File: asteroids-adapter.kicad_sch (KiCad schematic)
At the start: 15 parts, among them J1 Asteroids PCB connector, J2 Asteroids harness connector, U1 TL074

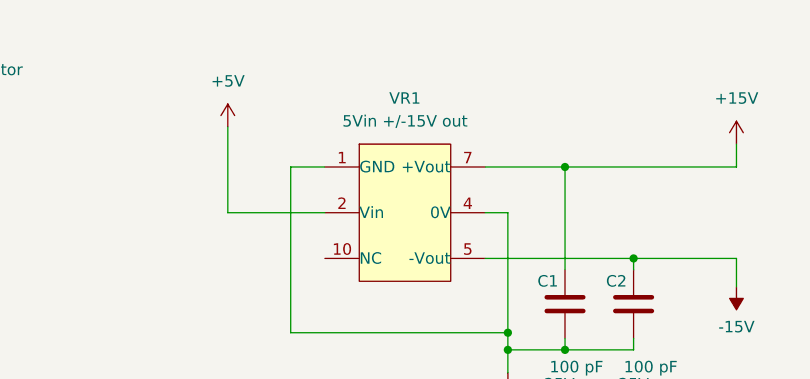
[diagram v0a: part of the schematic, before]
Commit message: Fixed DC-DC footprint and silk screen info
- Downloaded from CUI website

- fixed connector labels
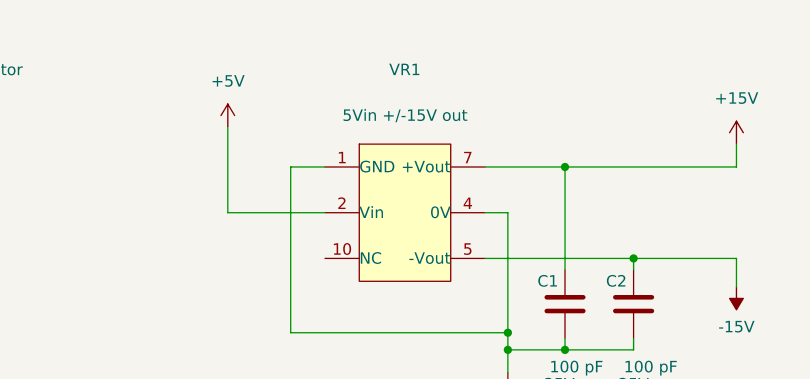
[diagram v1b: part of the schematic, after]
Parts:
- removed VR1: CUI PESE1-S5-D15-M 5V to +/-15V DC-DC converter 3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, asteroids-adapter:CUI PESE1 DC-DC dual out, symbol ast-adapter:CUI PESE1-S5-D15-M 5V to +/-15V DC-DC converter 34 mA
- added VR1: CUI PESE1-S5-D15-M, asteroids-adapter:CONV_PESE1-S5-D15-M, symbol ast-adapter:CUI PESE1-S5-D15-M
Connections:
- net +15V: now also VR1.7 (+Vout)
- net +5V: now also VR1.2 (Vin)
- net -15V: now also VR1.5 (-Vout)
- net GND: now also VR1.1 (GND), VR1.4 (0V)
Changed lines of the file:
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@@
     (pin "2")
-  )
-  (symbol (lib_id "ast-adapter:CUI PESE1-S5-D15-M 5V to +{slash}-15V DC-DC converter 34 mA") (at 151.765 34.925 0) (unit 1)
-    (in_bom yes) (on_board yes) (fields_autoplaced)
-    (property "Reference" "VR1" (id 0) (at 151.765 22.225 0))
-    (property "Value" "CUI PESE1-S5-D15-M 5V to +/-15V DC-DC converter 34 mA" (id 1) (at 126.365 140.843 0)
-      (effects (font (size 1.27 1.27)) (justify left) hide)
-    )
-    (property "Footprint" "asteroids-adapter:CUI PESE1 DC-DC dual out" (id 2) (at 151.765 22.225 0)
-      (effects (font (size 1.27 1.27)) hide)
-    )
-    (property "Datasheet" "https://www.google.com/url?sa=t&rct=j&q=&esrc=s&source=web&cd=&ved=2ahUKEwikiImr1v71AhUpk2oFHTgCD7YQFnoECAsQAQ&url=https%3A%2F%2Fwww.cui.com%2Fproduct%2Fresource%2Fpese1-m.pdf&usg=AOvVaw32_tGXML3NiDlAvSu1C1ul" (id 3) (at 128.143 135.509 0)
-      (effects (font (size 1.27 1.27)) hide)
-    )
-    (property "Component Value" "5Vin +/-15V out" (id 4) (at 151.765 24.765 0))
-    (property "Tolerance" "" (id 5) (at 132.207 145.669 0)
-      (effects (font (size 1.27 1.27)) hide)
-    )
-    (property "Manufacturer" "CUI" (id 6) (at 128.143 124.333 0)
-      (effects (font (size 1.27 1.27)) hide)
-    )
-    (property "Manufacturer Link" "https://www.cui.com/product/dc-dc-converters/isolated/pese1-m-series" (id 7) (at 130.937 130.937 0)
-      (effects (font (size 1.27 1.27)) hide)
-    )
-    (property "RoHS Document Link" "https://www.cui.com/product/resource/material-compliance/pese1-m-series" (id 8) (at 131.191 170.815 0)
-      (effects (font (size 1.27 1.27)) hide)
-    )
-    (property "Manufacturer PN" "PESE1-5S-D12-M" (id 9) (at 130.429 127.889 0)
-      (effects (font (size 1.27 1.27)) hide)
-    )
-    (property "RoHS" "Yes" (id 10) (at 127.889 168.021 0)
-      (effects (font (size 1.27 1.27)) hide)
-    )
-    (property "Allow Substitution" "No" (id 11) (at 127.635 173.863 0)
-      (effects (font (size 1.27 1.27)) hide)
-    )
-    (property "Fitted" "Yes" (id 12) (at 128.651 178.689 0)
-      (effects (font (size 1.27 1.27)) hide)
-    )
-    (property "Tracking" "No" (id 13) (at 128.143 176.149 0)
-      (effects (font (size 1.27 1.27)) hide)
-    )
-    (property "BOM Comment" "" (id 14) (at 154.305 106.045 0)
-      (effects (font (size 1.27 1.27)) hide)
-    )
-    (property "Component Type" "DC-DC converter" (id 15) (at 149.733 142.875 0)
-      (effects (font (size 1.27 1.27)) hide)
-    )
-    (property "Package Type" "SMT" (id 16) (at 116.205 121.285 0)
-      (effects (font (size 1.27 1.27)) hide)
-    )
-    (property "Package Variant" "" (id 17) (at 154.305 106.045 0)
-      (effects (font (size 1.27 1.27)) hide)
-    )
-    (property "Number of Pins" "If applicable" (id 18) (at 132.207 148.209 0)
-      (effects (font (size 1.27 1.27)) hide)
-    )
-    (property "Temp (Storage)" "If applicable" (id 19) (at 132.207 150.241 0)
-      (effects (font (size 1.27 1.27)) hide)
-    )
-    (property "Temp (Operating)" "If applicable" (id 20) (at 132.461 152.781 0)
-      (effects (font (size 1.27 1.27)) hide)
-    )
-    (property "Temp (Soldering)" "If applicable" (id 21) (at 132.461 155.575 0)
-      (effects (font (size 1.27 1.27)) hide)
-    )
-    (property "Temp Coeff." "If applicable" (id 22) (at 132.461 158.115 0)
-      (effects (font (size 1.27 1.27)) hide)
-    )
-    (property "Power Rating" "If applicable" (id 23) (at 132.461 160.655 0)
-      (effects (font (size 1.27 1.27)) hide)
-    )
-    (property "Material" "If applicable" (id 24) (at 132.461 162.941 0)
-      (effects (font (size 1.27 1.27)) hide)
-    )
-    (property "Class" "If applicable" (id 25) (at 132.461 165.227 0)
-      (effects (font (size 1.27 1.27)) hide)
-    )
-    (property "Standards Version" "1.1" (id 26) (at 128.651 181.737 0)
-      (effects (font (size 1.27 1.27)) hide)
-    )
-    (pin "1")
-    (pin "10")
-    (pin "2")
-    (pin "4")
-    (pin "5")
-    (pin "7")
   )
   (symbol (lib_id "power:GND") (at 104.775 170.18 0) (unit 1)
@@
     (pin "Z")
   )
+  (symbol (lib_id "ast-adapter:CUI PESE1-S5-D15-M") (at 151.765 34.925 0) (unit 1)
+    (in_bom yes) (on_board yes) (fields_autoplaced)
+    (property "Reference" "VR1" (id 0) (at 151.765 19.05 0))
+    (property "Value" "CUI PESE1-S5-D15-M" (id 1) (at 126.365 140.843 0)
+      (effects (font (size 1.27 1.27)) (justify left) hide)
+    )
+    (property "Footprint" "asteroids-adapter:CONV_PESE1-S5-D15-M" (id 2) (at 151.765 21.59 0)
+      (effects (font (size 1.27 1.27)) hide)
+    )
+    (property "Datasheet" "https://www.google.com/url?sa=t&rct=j&q=&esrc=s&source=web&cd=&ved=2ahUKEwikiImr1v71AhUpk2oFHTgCD7YQFnoECAsQAQ&url=https%3A%2F%2Fwww.cui.com%2Fproduct%2Fresource%2Fpese1-m.pdf&usg=AOvVaw32_tGXML3NiDlAvSu1C1ul" (id 3) (at 128.143 135.509 0)
+      (effects (font (size 1.27 1.27)) hide)
+    )
+    (property "Component Value" "5Vin +/-15V out" (id 4) (at 151.765 24.13 0))
+    (property "Tolerance" "" (id 5) (at 132.207 145.669 0)
+      (effects (font (size 1.27 1.27)) hide)
+    )
+    (property "Manufacturer" "CUI" (id 6) (at 128.143 124.333 0)
+      (effects (font (size 1.27 1.27)) hide)
+    )
+    (property "Manufacturer Link" "https://www.cui.com/product/dc-dc-converters/isolated/pese1-m-series" (id 7) (at 130.937 130.937 0)
+      (effects (font (size 1.27 1.27)) hide)
+    )
+    (property "RoHS Document Link" "https://www.cui.com/product/resource/material-compliance/pese1-m-series" (id 8) (at 131.191 170.815 0)
+      (effects (font (size 1.27 1.27)) hide)
+    )
+    (property "Manufacturer PN" "PESE1-5S-D12-M" (id 9) (at 130.429 127.889 0)
+      (effects (font (size 1.27 1.27)) hide)
+    )
+    (property "RoHS" "Yes" (id 10) (at 127.889 168.021 0)
+      (effects (font (size 1.27 1.27)) hide)
+    )
+    (property "Allow Substitution" "No" (id 11) (at 127.635 173.863 0)
+      (effects (font (size 1.27 1.27)) hide)
+    )
+    (property "Fitted" "Yes" (id 12) (at 128.651 178.689 0)
+      (effects (font (size 1.27 1.27)) hide)
+    )
+    (property "Tracking" "No" (id 13) (at 128.143 176.149 0)
+      (effects (font (size 1.27 1.27)) hide)
+    )
+    (property "BOM Comment" "" (id 14) (at 154.305 106.045 0)
+      (effects (font (size 1.27 1.27)) hide)
+    )
+    (property "Component Type" "DC-DC converter" (id 15) (at 149.733 142.875 0)
+      (effects (font (size 1.27 1.27)) hide)
+    )
+    (property "Package Type" "SMT" (id 16) (at 116.205 121.285 0)
+      (effects (font (size 1.27 1.27)) hide)
+    )
+    (property "Package Variant" "" (id 17) (at 154.305 106.045 0)
+      (effects (font (size 1.27 1.27)) hide)
+    )
+    (property "Number of Pins" "If applicable" (id 18) (at 132.207 148.209 0)
+      (effects (font (size 1.27 1.27)) hide)
+    )
+    (property "Temp (Storage)" "If applicable" (id 19) (at 132.207 150.241 0)
+      (effects (font (size 1.27 1.27)) hide)
+    )
+    (property "Temp (Operating)" "If applicable" (id 20) (at 132.461 152.781 0)
+      (effects (font (size 1.27 1.27)) hide)
+    )
+    (property "Temp (Soldering)" "If applicable" (id 21) (at 132.461 155.575 0)
+      (effects (font (size 1.27 1.27)) hide)
+    )
+    (property "Temp Coeff." "If applicable" (id 22) (at 132.461 158.115 0)
+      (effects (font (size 1.27 1.27)) hide)
+    )
+    (property "Power Rating" "If applicable" (id 23) (at 132.461 160.655 0)
+      (effects (font (size 1.27 1.27)) hide)
+    )
+    (property "Material" "If applicable" (id 24) (at 132.461 162.941 0)
+      (effects (font (size 1.27 1.27)) hide)
+    )
+    (property "Class" "If applicable" (id 25) (at 132.461 165.227 0)
+      (effects (font (size 1.27 1.27)) hide)
+    )
+    (property "Standards Version" "1.1" (id 26) (at 128.651 181.737 0)
+      (effects (font (size 1.27 1.27)) hide)
+    )
+    (pin "1")
+    (pin "10")
+    (pin "2")
+    (pin "4")
+    (pin "5")
+    (pin "7")
+  )
   (symbol (lib_id "ast-adapter:Yageo 10K ohm 1% thin film TH") (at 170.815 83.82 0) (unit 1)
     (in_bom yes) (on_board yes)
@@
       (reference "U1") (unit 5) (value "TL074") (footprint "Package_DIP:DIP-14_W7.62mm_LongPads")
     )
-    (path "/54237acd-3b11-4002-b44c-ec7678c2907b"
-      (reference "VR1") (unit 1) (value "CUI PESE1-S5-D15-M 5V to +/-15V DC-DC converter 34 mA") (footprint "asteroids-adapter:CUI PESE1 DC-DC dual out")
-    )
-  )
+    (path "/ac8d8548-4df8-4c39-8021-1ae8f0fd4c70"
+      (reference "VR1") (unit 1) (value "CUI PESE1-S5-D15-M") (footprint "asteroids-adapter:CONV_PESE1-S5-D15-M")
+    )
+  )

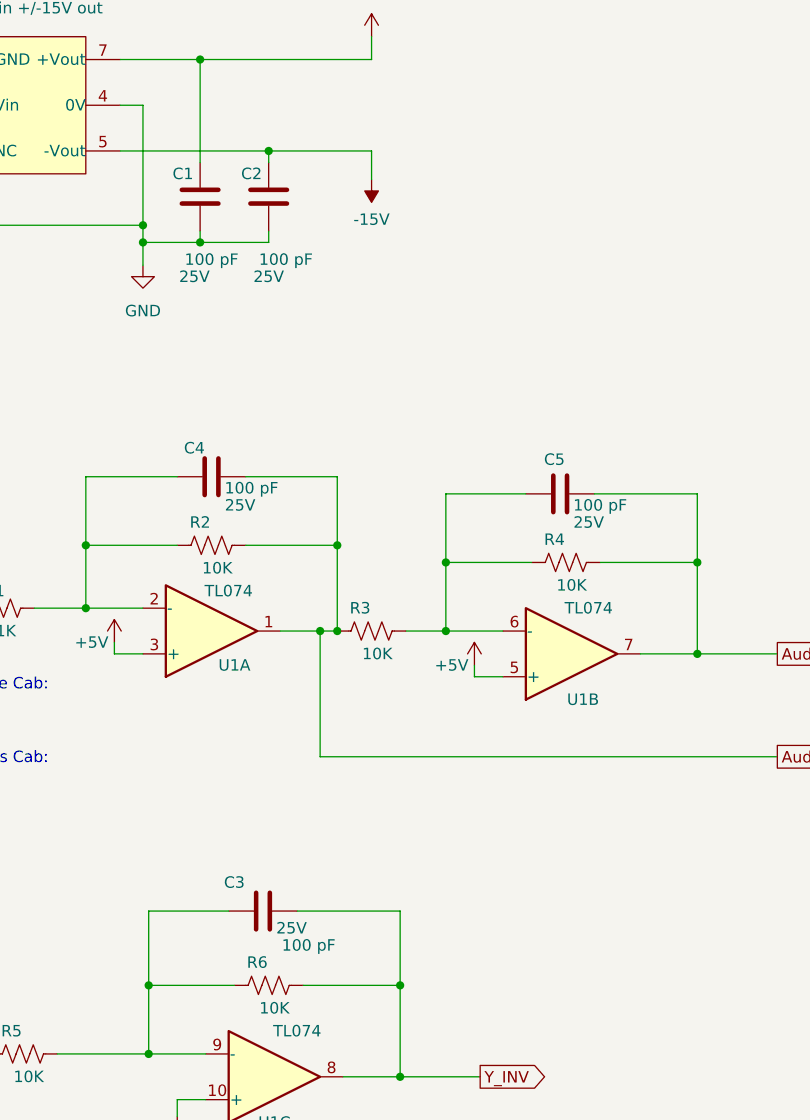
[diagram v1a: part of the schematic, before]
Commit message: Make sure all the caps have library symbols
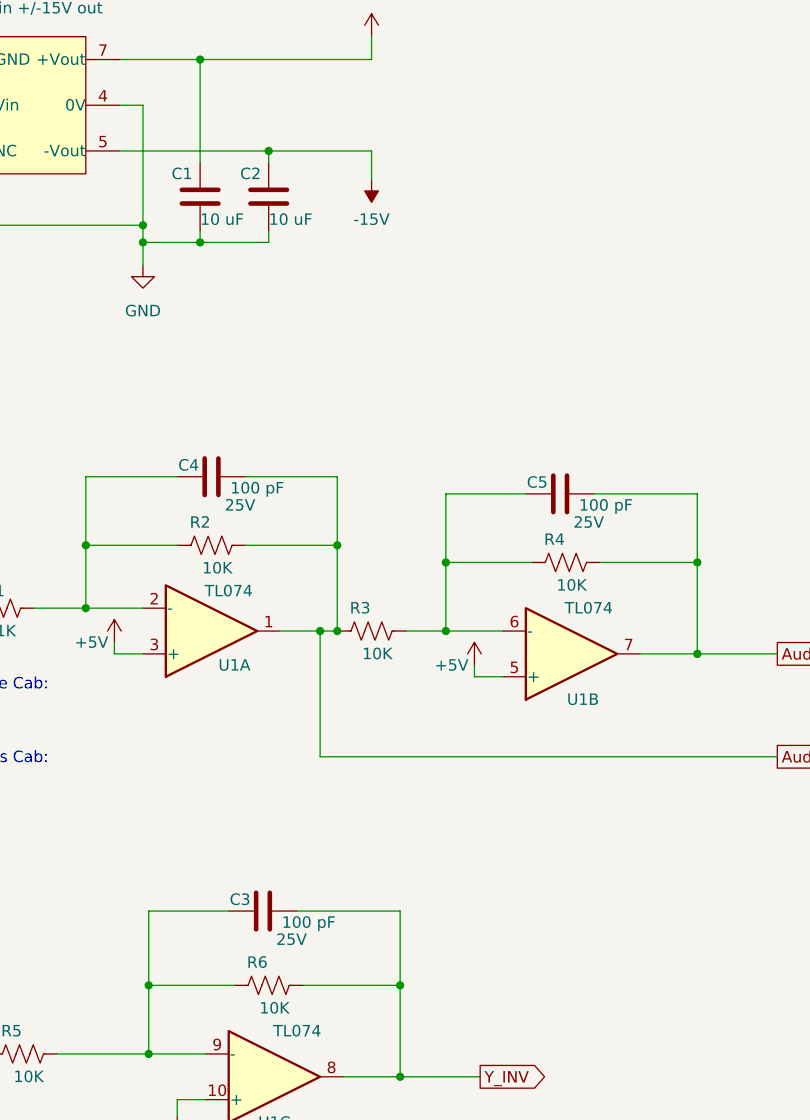
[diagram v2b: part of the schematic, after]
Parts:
- removed C1, C2, C3, C4, C5: Kemet MLCC 100 pF 5% 25V TH, Capacitor_THT:C_Disc_D3.0mm_W1.6mm_P2.50mm, symbol Isopoint: MuRata MLCC 22 uF 20% 16 V 0805
- added C1, C2: Kemet 10 uF 25V MLCC TH, Capacitor_THT:C_Disc_D3.0mm_W1.6mm_P2.50mm, symbol ast-adapter:Kemet 10 uF 25V MLCC TH
- added C3, C4, C5: Kemet MLCC 100 pF 5% 25V TH, Capacitor_THT:C_Disc_D3.0mm_W1.6mm_P2.50mm, symbol ast-adapter: Kemet MLCC 100 pF 5% 25V TH
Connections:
- net +15V: now also C1.2
- net -15V: now also C2.2
- net Audio_1_out: now also C4.2
- net Audio_2_out: now also C5.2
- net GND: now also C1.1, C2.1
- net Y_INV: now also C3.2
- net at R1.1, R2.2, U1.2 (-): now also C4.1
- net at R5.1, R6.2, U1.9 (-): now also C3.1
- net at R3.1, R4.2, U1.6 (-): now also C5.1
